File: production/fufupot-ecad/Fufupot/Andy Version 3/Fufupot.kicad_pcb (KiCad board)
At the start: 4 copper layers, 116.8 x 124.5 mm, 62 parts, among them IC1 FOD3150, J1 Conn_01x04, J10 Conn_01x03, J11 Conn_01x03, J12 Conn_01x02, J13 Conn_01x03, J2 USB_B, J3 Conn_01x03, J4 Conn_01x02, J6 Conn_01x02, J7 Conn_01x02, J8 Conn_01x04, J9 Conn_01x02, SW1 SW_Push, SW2 SW_Push, U1 USBLC6-2SC6, U2 LM5165DRC, U3 FT232RL, U4 ATMEGA328P-PN, U5 STGP8NC60KD

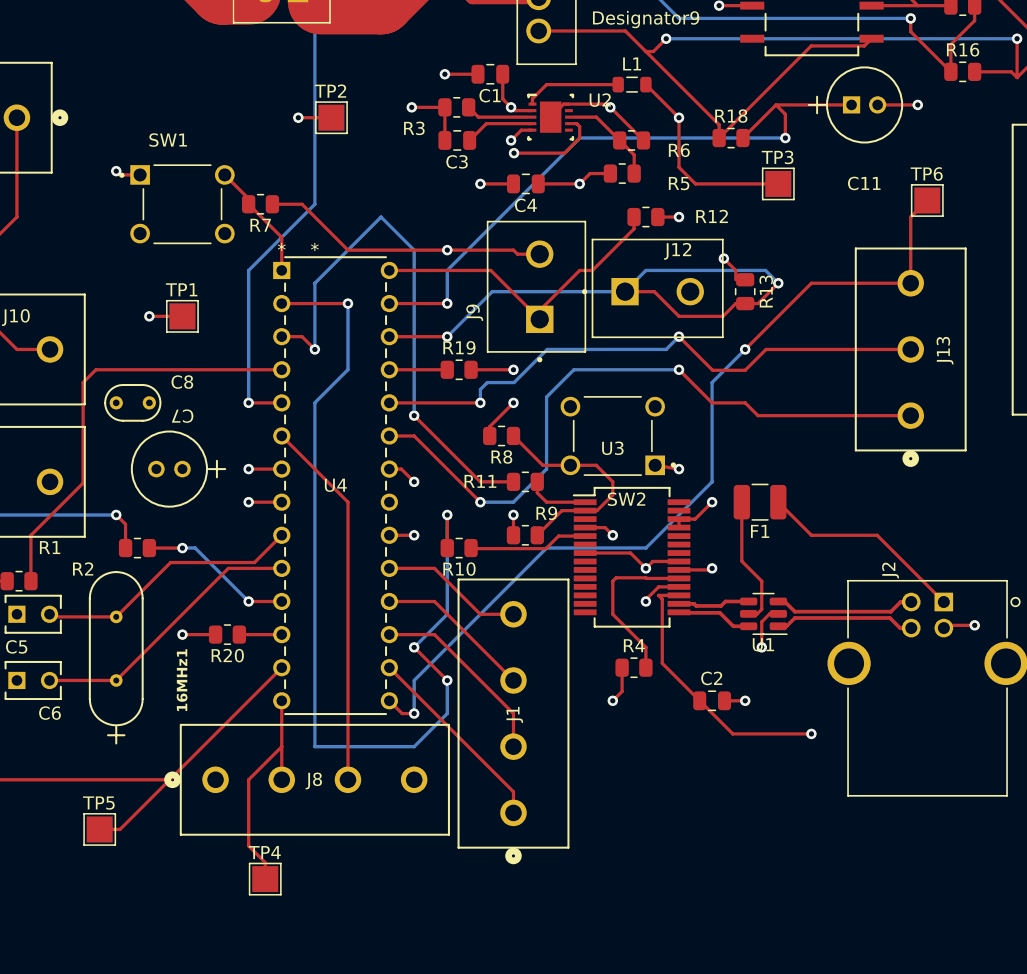
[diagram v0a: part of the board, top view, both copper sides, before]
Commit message: Added testpoints
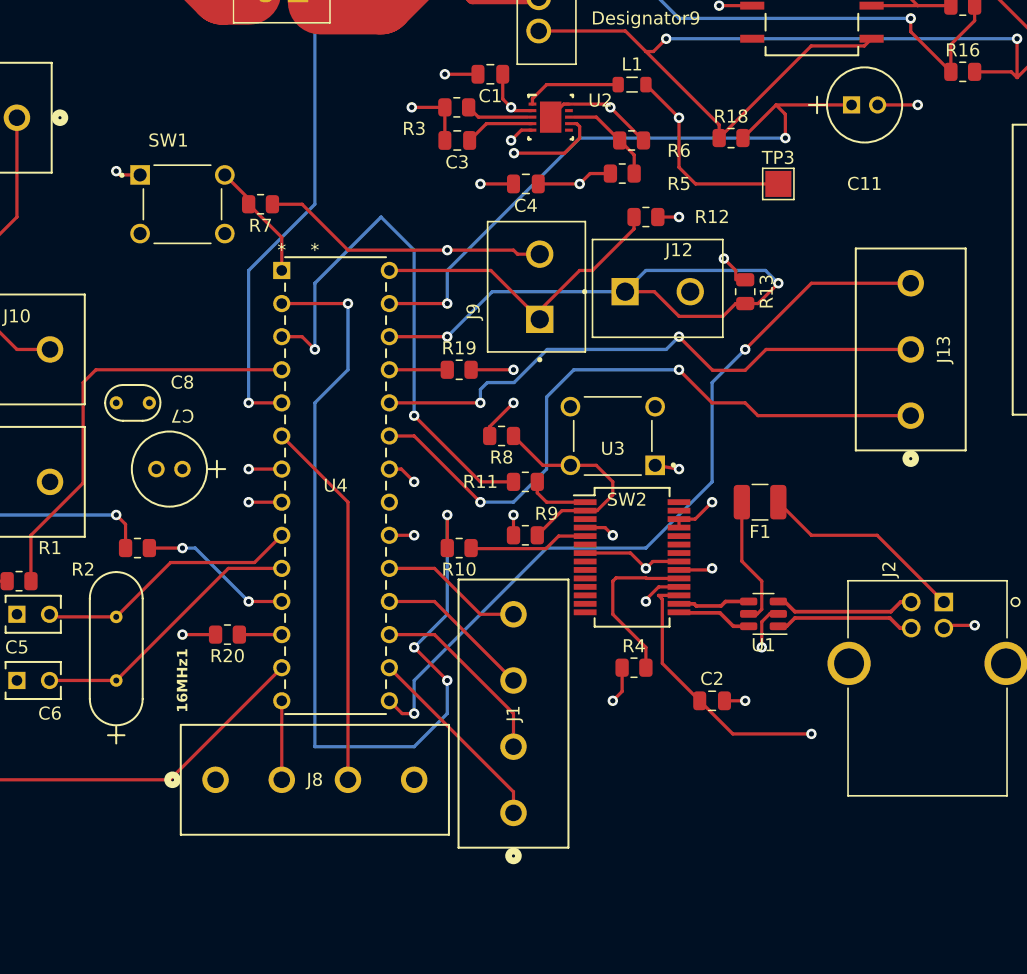
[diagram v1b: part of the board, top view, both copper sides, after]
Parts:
- removed TP1, TP2, TP4, TP5, TP6: TestPoint, TestPoint:TestPoint_Pad_2.0x2.0mm
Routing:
- net D_Switch: track 17.8 -> 6.06 mm
- net D_Buzz: track 41.7 -> 34.8 mm
- net PWM Speed Control: track 66.9 -> 60.0 mm
- net +48V: track 40.6 -> 38.1 mm, vias 7 -> 6
- net +5V: track 55.0 -> 52.4 mm, vias 10 -> 9
